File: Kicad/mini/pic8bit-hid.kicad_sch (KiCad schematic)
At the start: 43 parts, among them K301 HARWIN-254-F-1X08-VERTICAL, K302 HARWIN-254-F-1X06-VERTICAL, P301 10K, P302 10K, U301 CAT4002A, U302 MCP2221A

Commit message: Up
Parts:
- C301, C305, C307: symbol tronixio:KEMET-X7R-1206-10N-50V-20P -> tronixio:CAPACITOR-1206-10N-20P-X7R
- C302, C303, C304: symbol tronixio:KEMET-X7R-1206-1U-16V-20P -> tronixio:CAPACITOR-1206-1U-10P-X7R; Mouser 80-C1206C105M4R -> 80-C1206C105K5R; Tolerance 20% -> 10%; Voltage 16V -> 50V
- C306: symbol tronixio:KEMET-X7R-1206-100N-50V-20P -> tronixio:CAPACITOR-1206-100N-10P-X7R; Mouser 80-C1206C104M5R -> 80-C1206C104K5R; Tolerance 20% -> 10%
- R301, R303, R304, R307, R310, R311, R312, R313, R314, R315, R316, R317: symbol tronixio:KOASPEER-RK73B-1206-10K-5P -> tronixio:RESISTOR-1206-10K-5P
- R302, R305, R306, R309, R320: symbol tronixio:KOASPEER-RK73B-1206-1K-5P -> tronixio:RESISTOR-1206-1K-5P
- R308: symbol tronixio:KOASPEER-RK73B-1206-2K4-5P -> tronixio:RESISTOR-1206-2K4-5P
- R318, R319: symbol tronixio:KOASPEER-RK73B-1206-4K7-5P -> tronixio:RESISTOR-1206-4K7-5P

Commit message: Update
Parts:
- C302, C303, C304: Mouser 80-C1206C105K5R -> 80-C1206C105K4R; Voltage 50V -> 16V
- C306: Mouser 80-C1206C104K5R -> 187-CL31B106KAHNFNE
- S303: symbol tronixio:BOURNS-PEC12R-24DENTS-SWITCH -> tronixio:BOURNS-PEC12R-24-DENTS-SWITCH
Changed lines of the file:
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@@
     )
   )
-  (symbol (lib_id "tronixio:BOURNS-PEC12R-24DENTS-SWITCH") (at 165.1 139.7 0) (unit 1)
+  (symbol (lib_id "tronixio:BOURNS-PEC12R-24-DENTS-SWITCH") (at 165.1 139.7 0) (unit 1)
     (in_bom yes) (on_board yes) (dnp no)
     (property "Reference" "S303" (at 165.1 128.27 0)
@@
       (effects (font (size 1 1)) hide)
     )
-    (property "Voltage" "50V" (at 121.84 81.28 0) (do_not_autoplace)
+    (property "Voltage" "16V" (at 121.84 81.28 0) (do_not_autoplace)
       (effects (font (size 1.15 1.15)) (justify left) hide)
     )
@@
       (effects (font (size 1.15 1.15)) (justify left) hide)
     )
-    (property "Mouser" "80-C1206C105K5R" (at 116.84 88.9 0)
+    (property "Mouser" "80-C1206C105K4R" (at 116.84 88.9 0)
       (effects (font (size 1 1)) hide)
     )
@@
       (effects (font (size 1 1)) hide)
     )
-    (property "Voltage" "50V" (at 66.04 58.5 0) (do_not_autoplace)
+    (property "Voltage" "16V" (at 66.04 58.5 0) (do_not_autoplace)
       (effects (font (size 1.15 1.15)) (justify left) hide)
     )
@@
       (effects (font (size 1.15 1.15)) (justify left) hide)
     )
-    (property "Mouser" "80-C1206C105K5R" (at 73.66 63.5 0)
+    (property "Mouser" "80-C1206C105K4R" (at 73.66 63.5 0)
       (effects (font (size 1 1)) hide)
     )
@@
       (effects (font (size 1 1)) hide)
     )
-    (property "Voltage" "50V" (at 63.42 81.28 0) (do_not_autoplace)
+    (property "Voltage" "16V" (at 63.42 81.28 0) (do_not_autoplace)
       (effects (font (size 1.15 1.15)) (justify left) hide)
     )
@@
       (effects (font (size 1.15 1.15)) (justify left) hide)
     )
-    (property "Mouser" "80-C1206C105K5R" (at 58.42 88.9 0)
+    (property "Mouser" "80-C1206C105K4R" (at 58.42 88.9 0)
       (effects (font (size 1 1)) hide)
     )
@@
       (effects (font (size 1.15 1.15)) (justify left) hide)
     )
-    (property "Mouser" "80-C1206C104K5R" (at 172.72 88.9 0)
-      (effects (font (size 1 1)) hide)
-    )
+    (property "Mouser" "187-CL31B106KAHNFNE" (at 172.72 88.9 0)
+      (effects (font (size 1 1)) hide)
+    )

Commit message: Up
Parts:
- C301, C305, C307: symbol tronixio:CAPACITOR-1206-10N-20P-X7R -> tronixio:CAPACITOR-1206-10N-100V-5P-X7R; Mouser 80-C1206C103M5R -> 80-C1206C103J1R; Tolerance 20% -> 5%; Voltage 50V -> 100V
- C302, C303, C304: symbol tronixio:CAPACITOR-1206-1U-10P-X7R -> tronixio:CAPACITOR-1206-1U-16V-10P-X7R
- C306: symbol tronixio:CAPACITOR-1206-100N-10P-X7R -> tronixio:CAPACITOR-1206-100N-50V-5P-X7R; Mouser 187-CL31B106KAHNFNE -> 80-C1206C104J5R; Tolerance 10% -> 5%
- K301: footprint tronixio:HARWIN-M20-782084x -> tronixio:HARWIN-M20-782064x; Mouser 855-M20-999084 -> 855-M20-782064
- P301, P302, R301, R303, R304, R307, R310, R311, R312, R313, R314, R316, R317: value 10K -> 10k
- R302, R305, R306, R309, R320: value 1K -> 1k
- R308: value 2K4 -> 2k4
- R315: value 1K -> 10k
- R318, R319: value 4K7 -> 4k7
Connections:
- net GND: now also S303.5; no longer S303.4
- net at R309.2, R312.2: now also S303.4; no longer S303.5
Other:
- moved on the sheet: C302, C303, C305, C306, JP302, JP303, LCD301, LED301, LED302, R309, R310, R311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

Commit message: Up
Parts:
- K301: footprint tronixio:HARWIN-M20-782064x -> tronixio:HARWIN-M20-782084x; Mouser 855-M20-782064 -> 855-M20-782084
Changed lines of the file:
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@@
       (effects (font (size 1.15 1.15)) hide)
     )
-    (property "Footprint" "tronixio:HARWIN-M20-782064x" (at 99.06 157.48 0) (do_not_autoplace)
+    (property "Footprint" "tronixio:HARWIN-M20-782084x" (at 99.06 157.48 0) (do_not_autoplace)
       (effects (font (size 1 1)) hide)
     )
-    (property "Datasheet" "https://www.harwin.com/products/M20-7820646/" (at 99.06 160.02 0) (do_not_autoplace)
+    (property "Datasheet" "https://www.harwin.com/products/M20-7820846/" (at 99.06 160.02 0) (do_not_autoplace)
       (effects (font (size 1 1)) hide)
     )
-    (property "Mouser" "855-M20-782064" (at 99.06 162.56 0) (do_not_autoplace)
+    (property "Mouser" "855-M20-782084" (at 99.06 162.56 0) (do_not_autoplace)
       (effects (font (size 1 1)) hide)
     )

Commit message: Update Mini Kicad 8
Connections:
- net +3V3 renamed POWER-+3V3
- net +5V renamed POWER-+5V
- net GND renamed POWER-GND

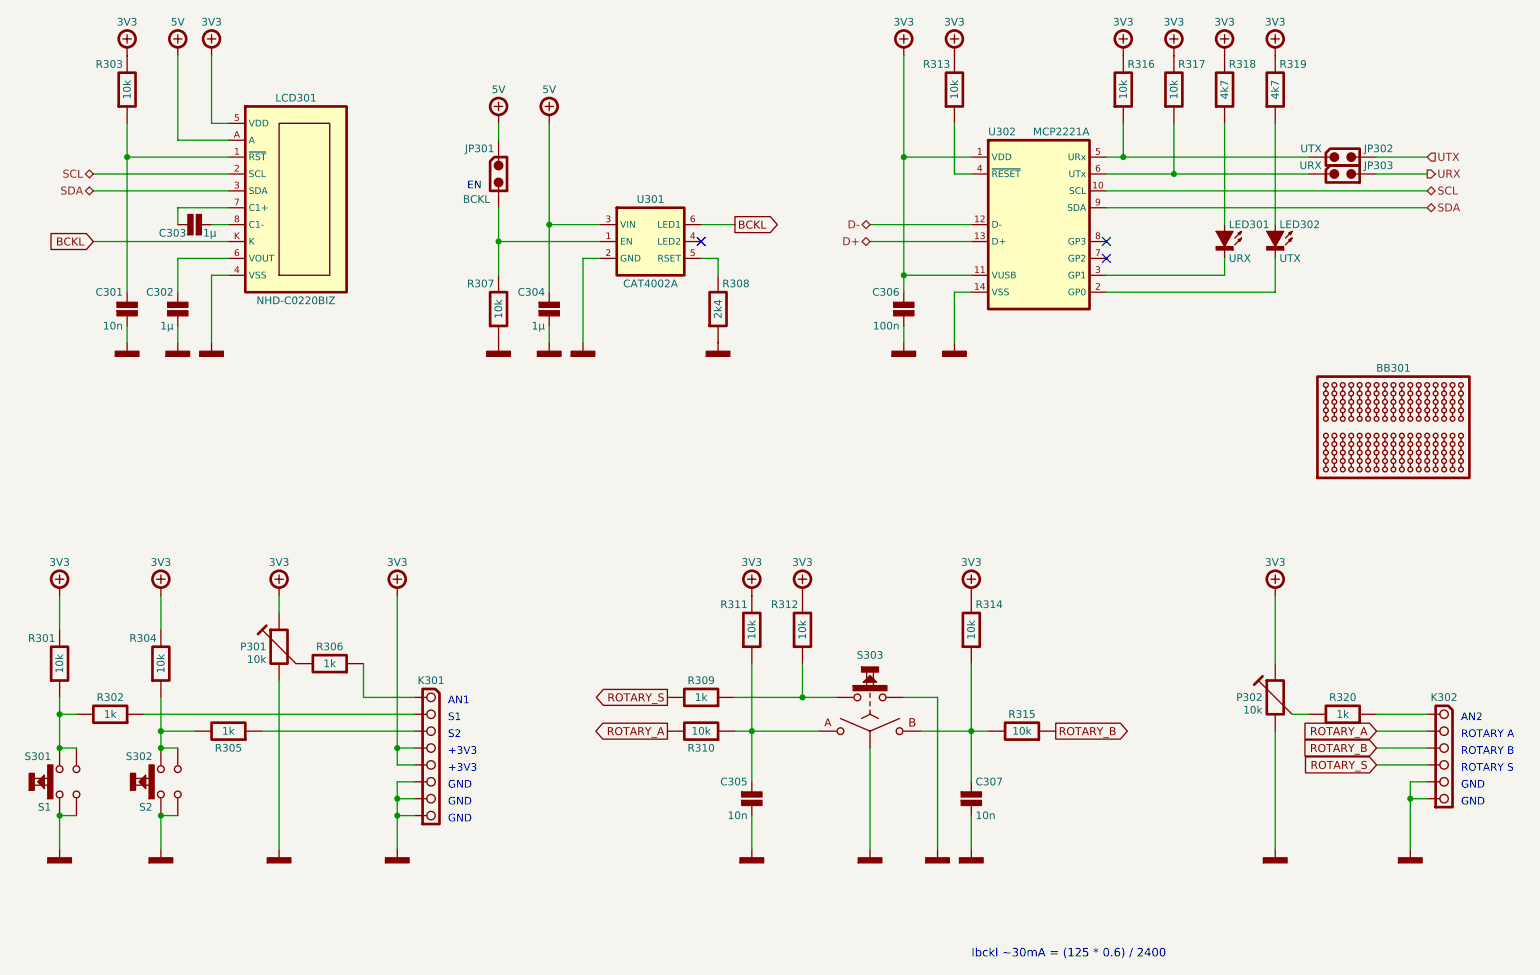
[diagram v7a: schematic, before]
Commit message: Update Nano & Mini
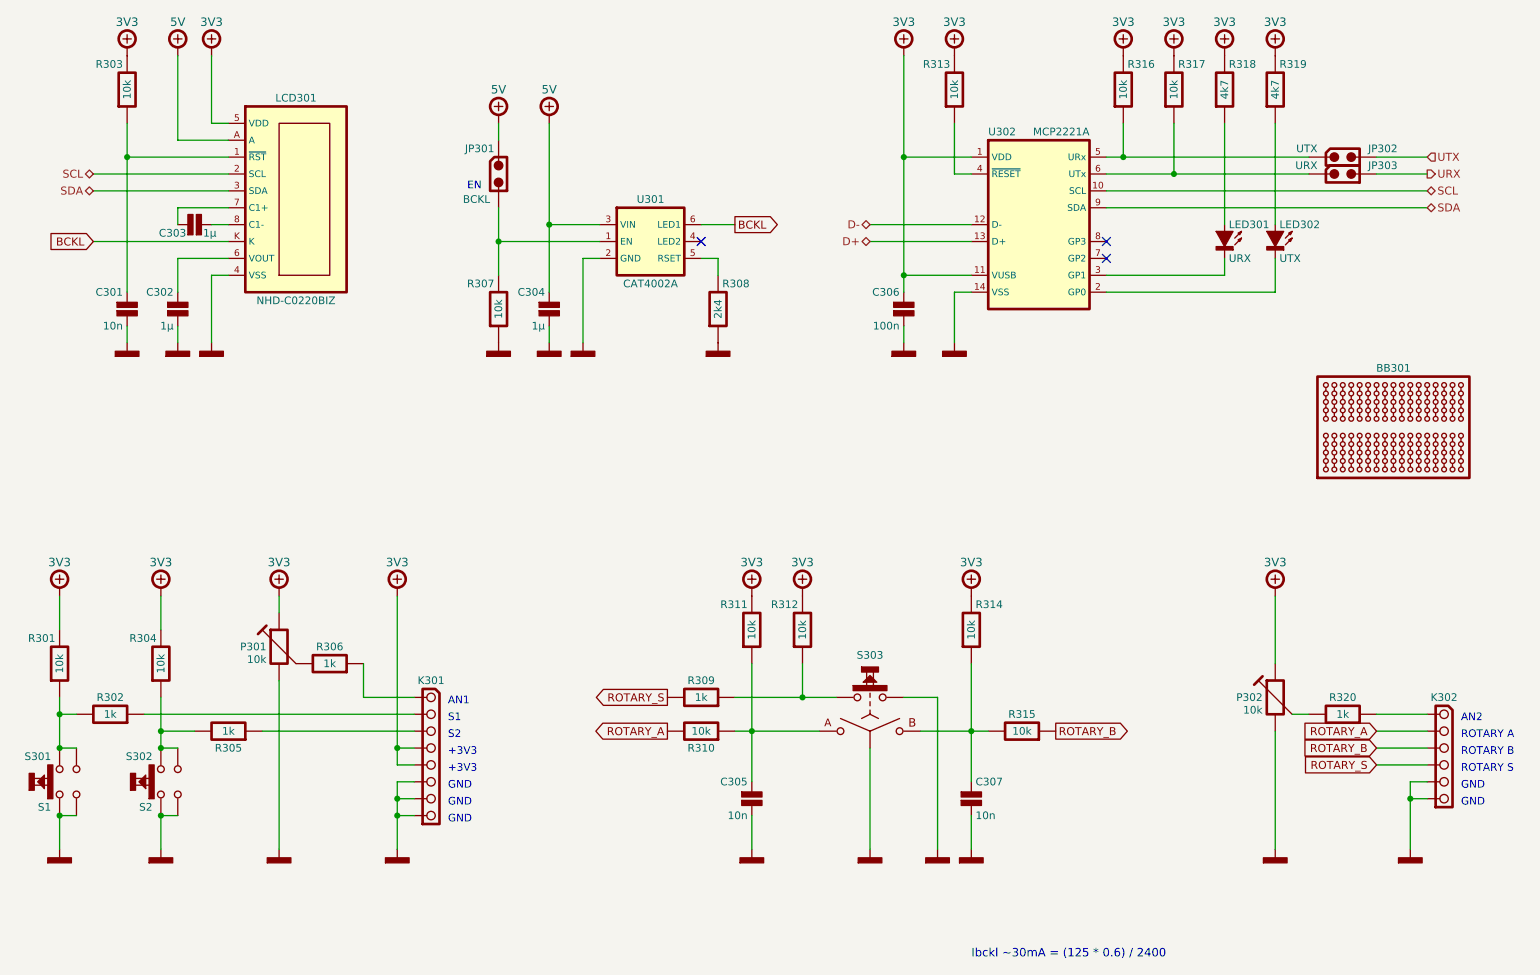
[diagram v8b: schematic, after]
